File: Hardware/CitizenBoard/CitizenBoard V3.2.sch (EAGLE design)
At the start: 28 parts, among them IC1 MEGA8-P, J1 DCJ0202

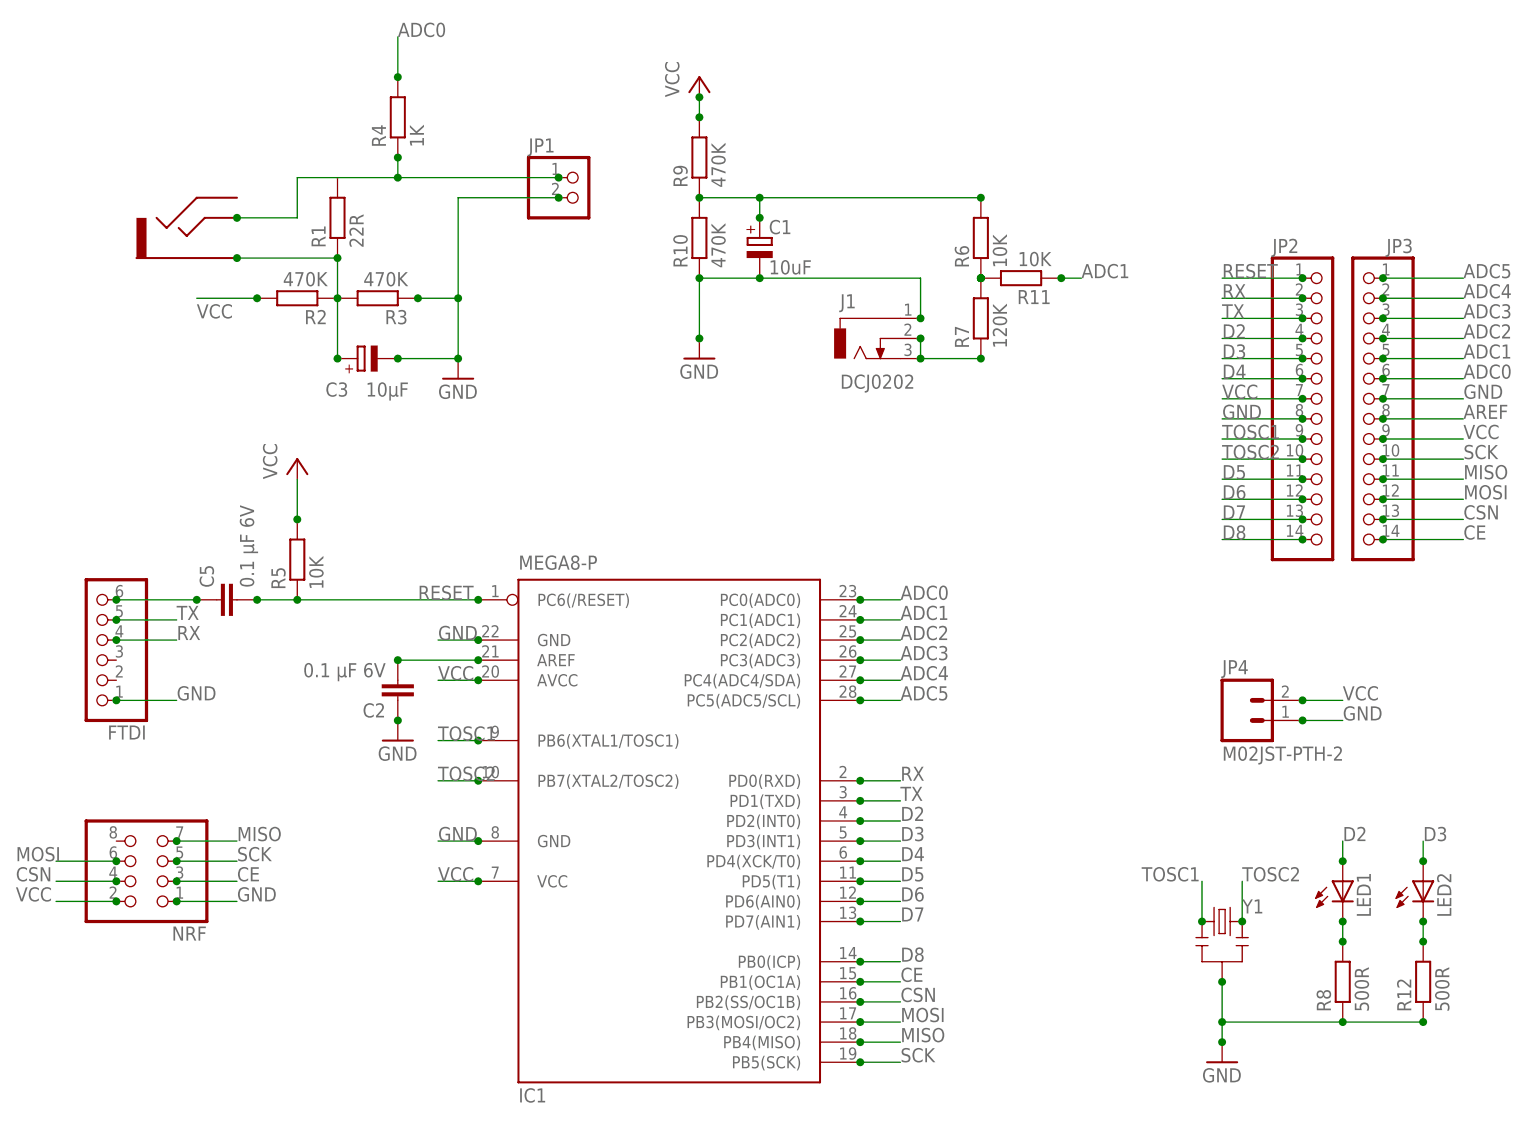
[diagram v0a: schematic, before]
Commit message: Board silk fix
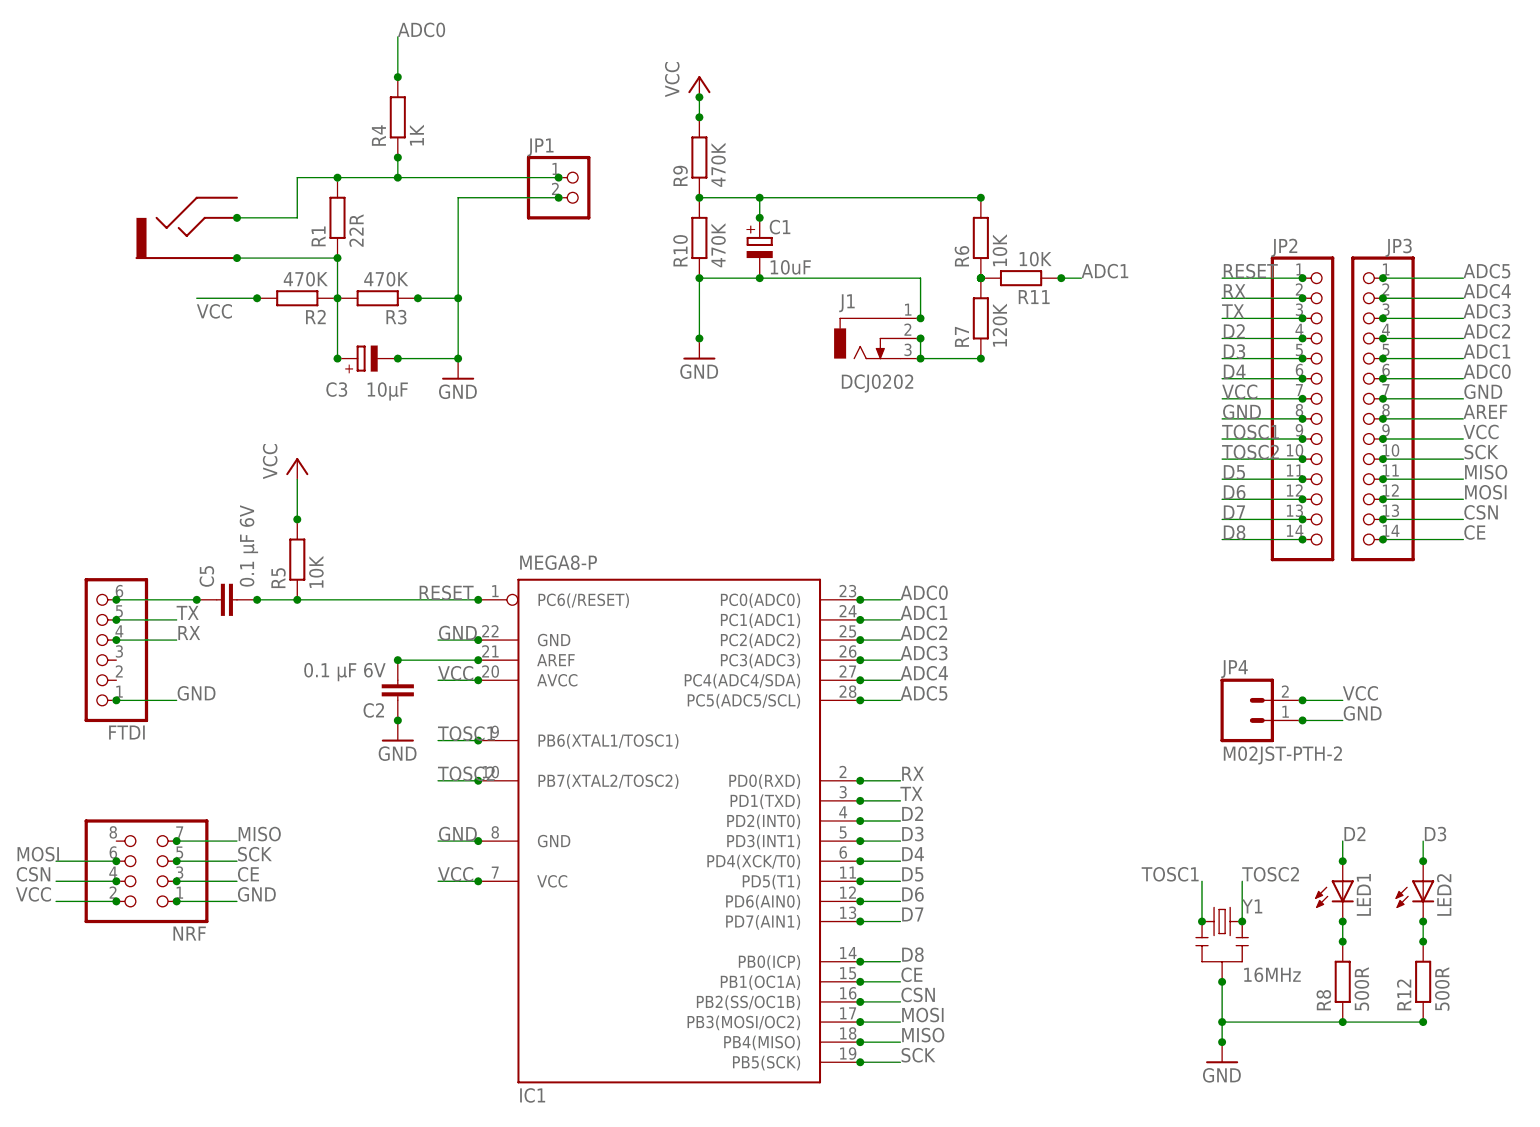
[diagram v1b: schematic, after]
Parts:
- Y1: value (none) -> 16MHz
- renumbered U$1 to J2
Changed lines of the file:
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@@
 <setting verticaltext="up"/>
 </settings>
-<grid distance="0.1" unitdist="inch" unit="inch" style="lines" multiple="1" display="yes" altdistance="0.01" altunitdist="inch" altunit="inch"/>
+<grid distance="0.1" unitdist="inch" unit="inch" style="lines" multiple="1" display="no" altdistance="0.01" altunitdist="inch" altunit="inch"/>
 <layers>
 <layer number="1" name="Top" color="4" fill="1" visible="no" active="no"/>
@@
 <part name="LED1" library="led" deviceset="LED" device="3MM"/>
 <part name="R8" library="rcl" deviceset="R-EU_" device="0204/7" value="500R"/>
-<part name="Y1" library="SparkFun-FreqCtrl" deviceset="RESONATOR" device="PTH"/>
+<part name="Y1" library="SparkFun-FreqCtrl" deviceset="RESONATOR" device="PTH" value="16MHz"/>
 <part name="FRAME1" library="SparkFun-Aesthetics" deviceset="FRAME-A4L" device=""/>
 <part name="JP4" library="SparkFun-Connectors" deviceset="M02" device="JST-PTH-2"/>
@@
 <part name="GND4" library="supply1" deviceset="GND" device=""/>
 <part name="P+2" library="supply1" deviceset="VCC" device=""/>
-<part name="U$1" library="alex" deviceset="AUDIO-JACK-3.5" device=""/>
+<part name="J2" library="alex" deviceset="AUDIO-JACK-3.5" device=""/>
 </parts>
 <sheets>
@@
 <instance part="GND4" gate="1" x="40.64" y="40.64"/>
 <instance part="P+2" gate="VCC" x="27.94" y="76.2"/>
-<instance part="U$1" gate="G$1" x="12.7" y="104.14"/>
+<instance part="J2" gate="G$1" x="12.7" y="104.14"/>
 </instances>
 <busses>
@@
 <junction x="33.02" y="101.6"/>
 <wire x1="33.02" y1="101.6" x2="20.32" y2="101.6" width="0.1524" layer="91"/>
-<pinref part="U$1" gate="G$1" pin="GND"/>
+<pinref part="J2" gate="G$1" pin="GND"/>
 <junction x="20.32" y="101.6"/>
 </segment>
@@
 <wire x1="27.94" y1="111.76" x2="27.94" y2="106.68" width="0.1524" layer="91"/>
 <wire x1="27.94" y1="106.68" x2="20.32" y2="106.68" width="0.1524" layer="91"/>
-<pinref part="U$1" gate="G$1" pin="L"/>
+<pinref part="J2" gate="G$1" pin="L"/>
 <junction x="20.32" y="106.68"/>
-</segment>
-</net>
+<junction x="33.02" y="111.76"/>
+</segment>
+</net>
